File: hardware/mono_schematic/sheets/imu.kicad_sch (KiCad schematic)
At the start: 5 parts

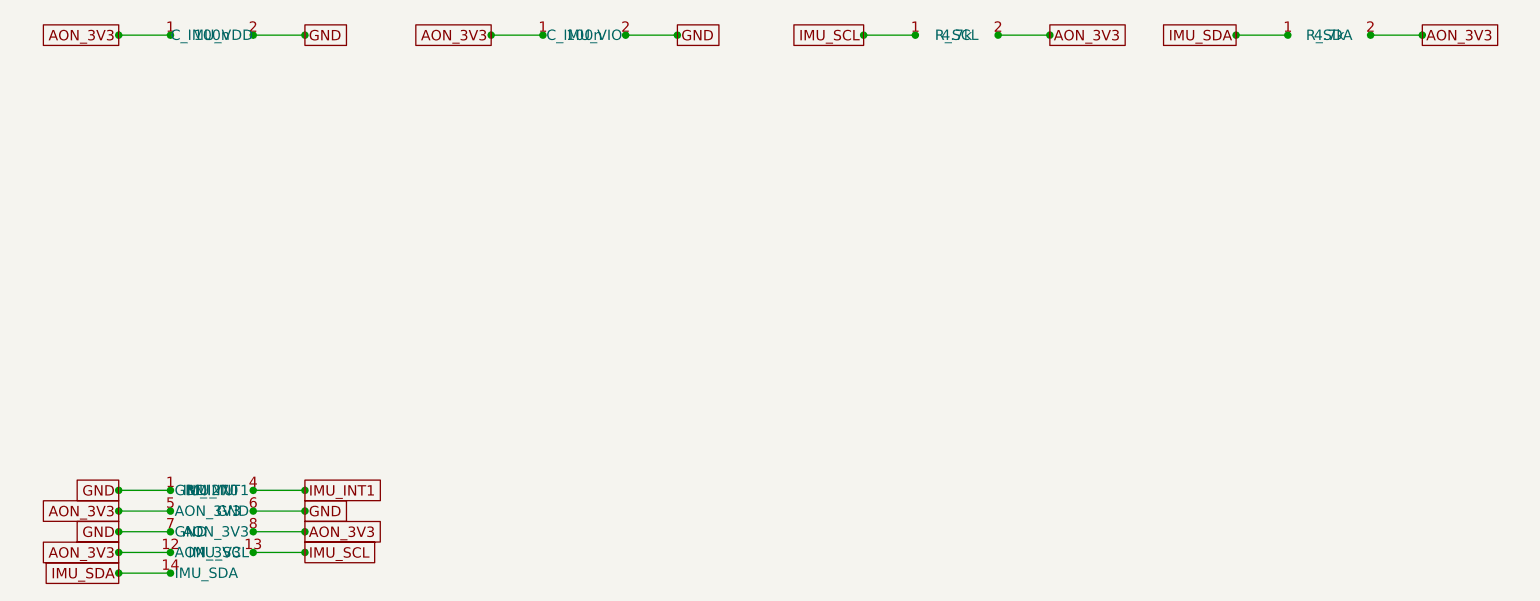
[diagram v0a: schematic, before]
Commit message: mono_electronics v11b: TLV75733P 1A AON LDO, 22uF ESP32 bulk, LED_EN RC glitch filter, J_USB value, refs end in digit; schematic regenerated (ERC 0, 0 diffs)
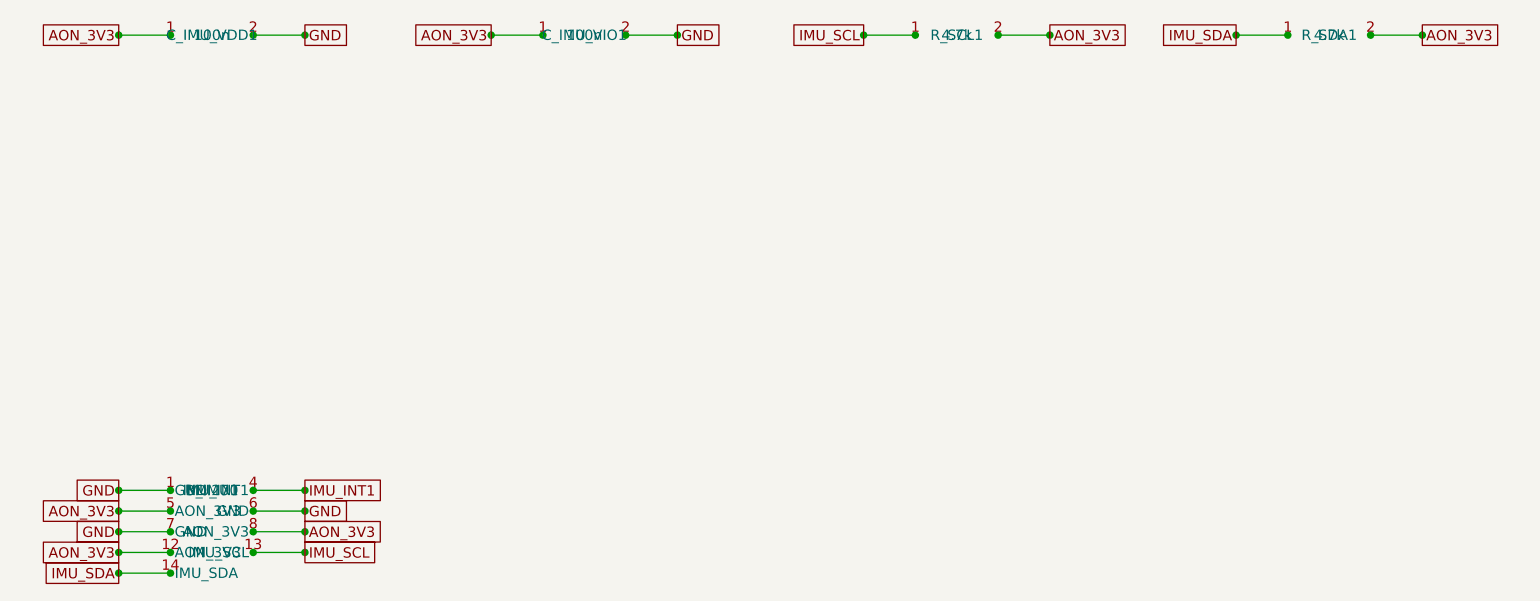
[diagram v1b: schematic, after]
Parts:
- removed C_IMU_VDD, C_IMU_VIO: 100n, mono_electronics:C_0402_1005Metric, symbol mono_parts:100n_C_0402_1005Metric_2
- removed R_SCL, R_SDA: 4.7k, mono_electronics:R_0402_1005Metric, symbol mono_parts:4.7k_R_0402_1005Metric_2
- removed U_IMU: BMI270, mono_electronics:Bosch_LGA-14_3x2.5mm_P0.5mm, symbol mono_parts:BMI270_Bosch_LGA-14_3x2.5mm_P0.5mm_9
- added C_IMU_VDD1, C_IMU_VIO1: 100n, mono_electronics:C_0402_1005Metric, symbol mono_parts:100n_C_0402_1005Metric_2
- added R_SCL1, R_SDA1: 4.7k, mono_electronics:R_0402_1005Metric, symbol mono_parts:4.7k_R_0402_1005Metric_2
- added U_IMU1: BMI270, mono_electronics:Bosch_LGA-14_3x2.5mm_P0.5mm, symbol mono_parts:BMI270_Bosch_LGA-14_3x2.5mm_P0.5mm_9
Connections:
- net AON_3V3: now also C_IMU_VDD1.1, C_IMU_VIO1.1, R_SCL1.2, R_SDA1.2, U_IMU1.12 (AON_3V3), U_IMU1.5 (AON_3V3), U_IMU1.8 (AON_3V3)
- net GND: now also C_IMU_VDD1.2, C_IMU_VIO1.2, U_IMU1.1 (GND), U_IMU1.6 (GND), U_IMU1.7 (GND)
- net IMU_INT1: now also U_IMU1.4 (IMU_INT1)
- net IMU_SCL: now also R_SCL1.1, U_IMU1.13 (IMU_SCL)
- net IMU_SDA: now also R_SDA1.1, U_IMU1.14 (IMU_SDA)
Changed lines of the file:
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@@
     (property
       "Reference"
-      "C_IMU_VDD"
+      "C_IMU_VDD1"
       (at 35.56 35.56 0)
       (effects
@@
     (instances
       (project "mono_electronics"
-        (path "/0b213b57-8f61-4d5e-b8ed-fca8ccca742d"
-          (reference "C_IMU_VDD")
+        (path "/258033f8-642a-45d8-bf5f-ae9ec14884e8"
+          (reference "C_IMU_VDD1")
           (unit 1)
         )
@@
     (property
       "Reference"
-      "C_IMU_VIO"
+      "C_IMU_VIO1"
       (at 81.28 35.56 0)
       (effects
@@
     (instances
       (project "mono_electronics"
-        (path "/0b213b57-8f61-4d5e-b8ed-fca8ccca742d"
-          (reference "C_IMU_VIO")
+        (path "/258033f8-642a-45d8-bf5f-ae9ec14884e8"
+          (reference "C_IMU_VIO1")
           (unit 1)
         )
@@
     (property
       "Reference"
-      "R_SCL"
+      "R_SCL1"
       (at 127 35.56 0)
       (effects
@@
     (instances
       (project "mono_electronics"
-        (path "/0b213b57-8f61-4d5e-b8ed-fca8ccca742d"
-          (reference "R_SCL")
+        (path "/258033f8-642a-45d8-bf5f-ae9ec14884e8"
+          (reference "R_SCL1")
           (unit 1)
         )
@@
     (property
       "Reference"
-      "R_SDA"
+      "R_SDA1"
       (at 172.72 35.56 0)
       (effects
@@
     (instances
       (project "mono_electronics"
-        (path "/0b213b57-8f61-4d5e-b8ed-fca8ccca742d"
-          (reference "R_SDA")
+        (path "/258033f8-642a-45d8-bf5f-ae9ec14884e8"
+          (reference "R_SDA1")
           (unit 1)
         )
@@
     (property
       "Reference"
-      "U_IMU"
+      "U_IMU1"
       (at 35.56 91.44 0)
       (effects
@@
     (instances
       (project "mono_electronics"
-        (path "/0b213b57-8f61-4d5e-b8ed-fca8ccca742d"
-          (reference "U_IMU")
+        (path "/258033f8-642a-45d8-bf5f-ae9ec14884e8"
+          (reference "U_IMU1")
           (unit 1)
         )
@@
   )
   (sheet_instances
-    (path "/0b213b57-8f61-4d5e-b8ed-fca8ccca742d"
+    (path "/258033f8-642a-45d8-bf5f-ae9ec14884e8"
       (page "1")
     )
